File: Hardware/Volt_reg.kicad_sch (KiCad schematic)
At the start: 45 parts, among them Q2 BSZ025N04LS, Q3 BSZ025N04LS, Q4 BUK9M11-40EX, Q5 BUK9M11-40EX, U10 TPS55288QRPMRQ1, U8 INA219AxDCN, U9 LM74810

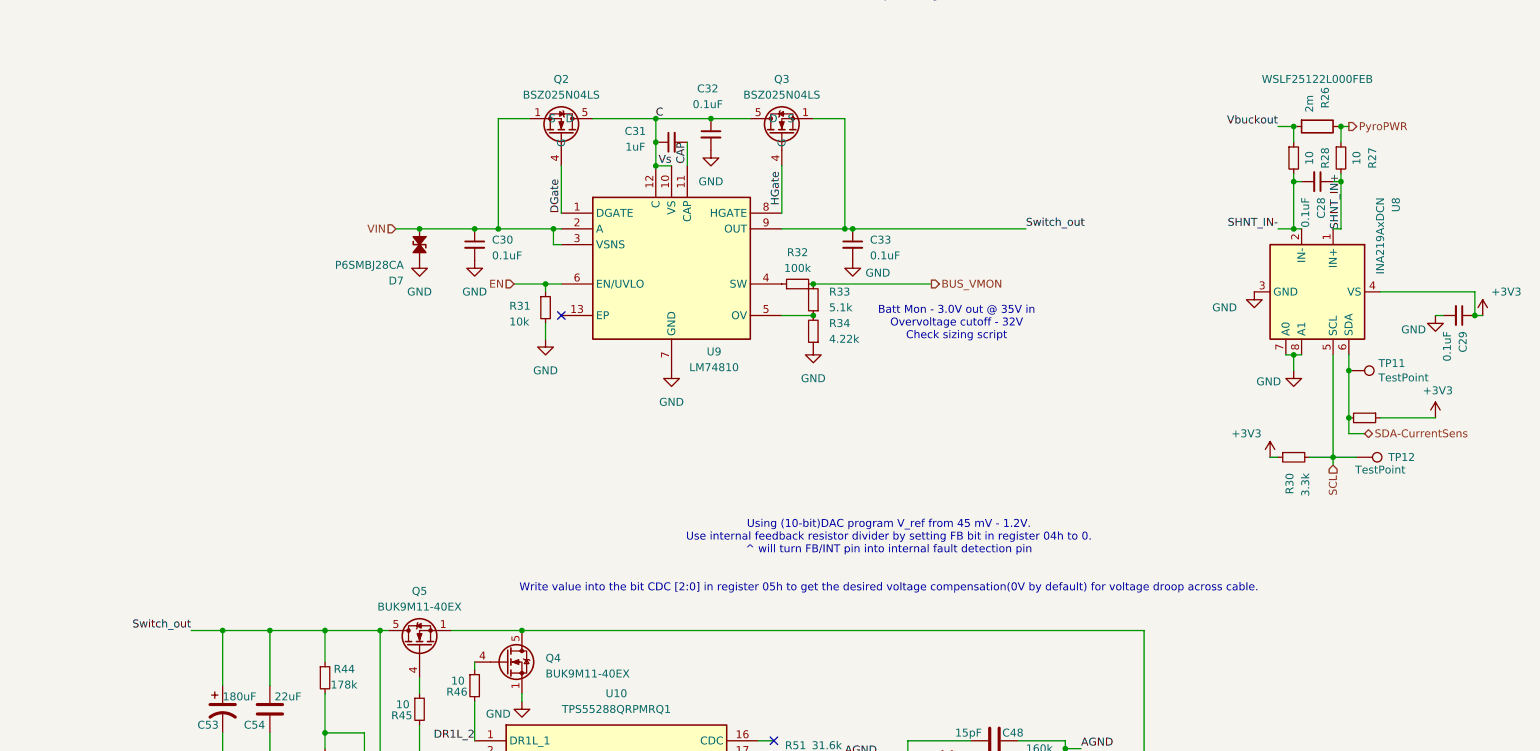
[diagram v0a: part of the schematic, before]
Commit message: Crosshair post review 2
Layout redesign + changes implemented. Traces not yet complete
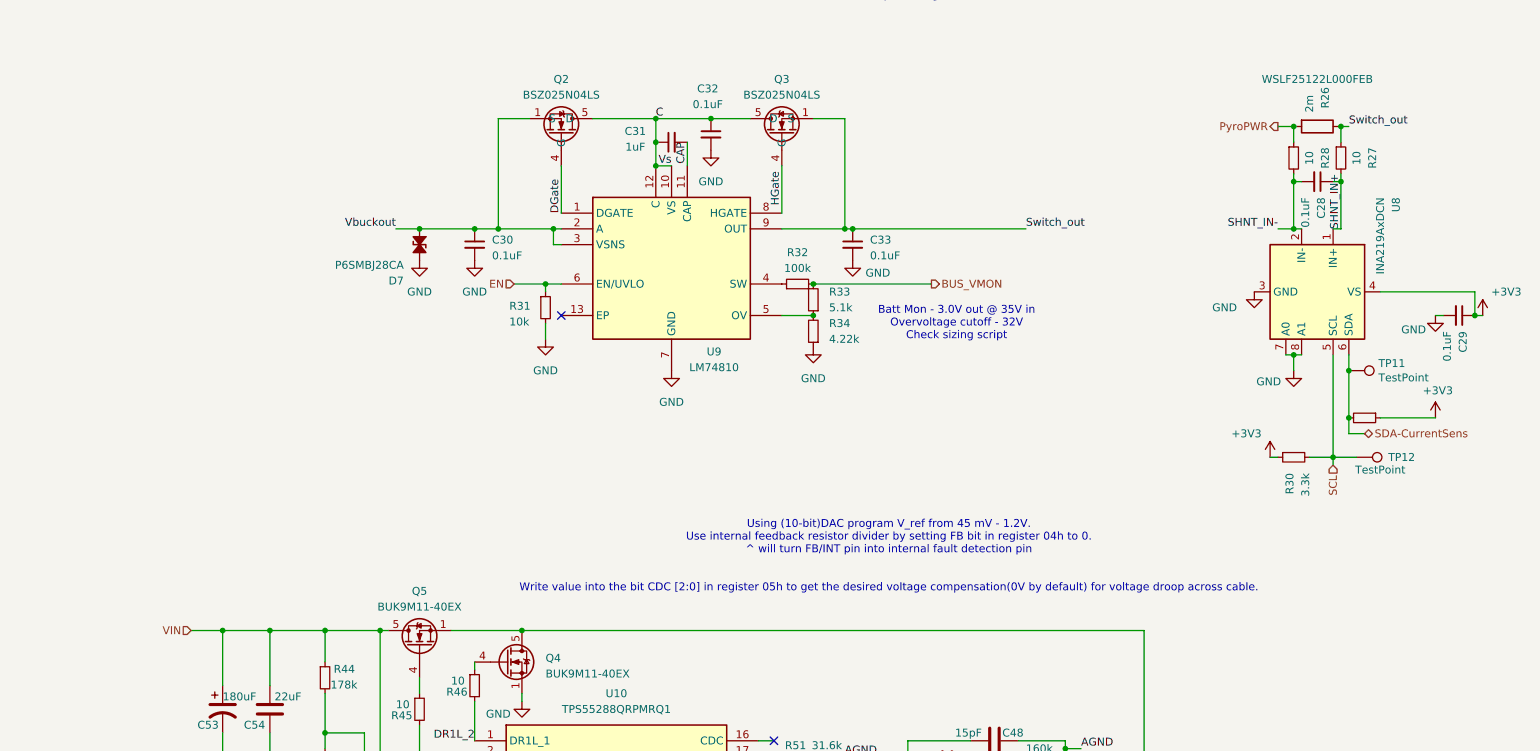
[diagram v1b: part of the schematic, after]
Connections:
- net ISN_2: now also C30.1, D7.1 (A1), Q2.1 (S), Q2.2 (S), Q2.3 (S), Q2.A1 (S), U9.2 (A), U9.3 (VSNS); no longer R26.2, R28.1
- net PyroPWR: now also R26.2, R28.1; no longer R26.1, R27.1
- net Switch_out: now also R26.1, R27.1; no longer C53.1, C54.2, Q5.5 (D), R44.1, U10.3 (VIN)
- net VIN: now also C53.1, C54.2, Q5.5 (D), R44.1, U10.3 (VIN); no longer C30.1, D7.1 (A1), Q2.1 (S), Q2.2 (S), Q2.3 (S), Q2.A1 (S), U9.2 (A), U9.3 (VSNS)
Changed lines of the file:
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@@
+		)
+	)
+	(label "Switch_out"
+		(at 213.36 55.88 0)
+		(effects
+			(font
+				(size 1.27 1.27)
+			)
+			(justify left bottom)
 		)
 	)
@@
 		)
 	)
-	(label "Vbuckout"
-		(at 201.93 55.88 180)
-		(effects
-			(font
-				(size 1.27 1.27)
-			)
-			(justify right bottom)
-		)
-	)
 	(label "DGate"
 		(at 86.36 69.85 90)
@@
 		)
 	)
-	(label "Switch_out"
-		(at 26.67 137.16 180)
-		(effects
-			(font
-				(size 1.27 1.27)
-			)
-			(justify right bottom)
-		)
-	)
 	(label "VCC_2"
 		(at 118.11 162.56 0)
@@
 			)
 			(justify left bottom)
+		)
+	)
+	(label "Vbuckout"
+		(at 59.69 72.39 180)
+		(effects
+			(font
+				(size 1.27 1.27)
+			)
+			(justify right bottom)
 		)
 	)
@@
 		)
 	)
-	(hierarchical_label "PyroPWR"
-		(shape output)
-		(at 213.36 55.88 0)
-		(effects
-			(font
-				(size 1.27 1.27)
-			)
-			(justify left)
-		)
-	)
 	(hierarchical_label "SDA-BuckBC"
 		(shape bidirectional)
@@
 	(hierarchical_label "VIN"
 		(shape input)
-		(at 59.69 72.39 180)
-		(effects
-			(font
+		(at 26.67 137.16 180)
+		(effects
+			(font
+				(size 1.27 1.27)
+			)
+			(justify right)
+		)
+	)
+	(hierarchical_label "PyroPWR"
+		(shape output)
+		(at 201.93 55.88 180)
+		(effects
+			(font

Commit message: Major changes made to layout
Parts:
- removed C30, C33: 0.1uF, Capacitor_SMD:C_0402_1005Metric, symbol Device:C_Small
- removed C31: 1uF, Capacitor_SMD:C_0402_1005Metric, symbol Device:C_Small
- removed C32: 0.1uF, Capacitor_SMD:C_0603_1608Metric, symbol Device:C_Small
- removed D7: P6SMBJ28CA, Diode_SMD:D_SMA, symbol Device:D_TVS_Small_Filled
- removed Q2, Q3: BSZ025N04LS, iclr:BSZ025N04LS, symbol iclr:BSZ025N04LS
- removed R31: 10k, Resistor_SMD:R_0402_1005Metric, symbol Device:R_Small
- removed R32: 100k, Resistor_SMD:R_0402_1005Metric, symbol Device:R_Small
- removed R33: 5.1k, Resistor_SMD:R_0402_1005Metric, symbol Device:R_Small
- removed R34: 4.22k, Resistor_SMD:R_0402_1005Metric, symbol Device:R_Small
- removed U9: LM74810, iclr:SON50P300X300X80-13N-D, symbol iclr:LM74810QDRRRQ1
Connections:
- net Switch_out is gone; now on net PyroPWR: R26.1, R27.1
- net ISN_2: now also R26.2, R28.1
- net PyroPWR: no longer R26.2, R28.1
- no-connect marks 2 -> 1
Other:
- note removed: "Batt Mon - 3.0V out @ 35V in Overvoltage cutoff - 32V Check sizing script"

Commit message: Saved changes
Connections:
- net ISN_2: now also R26.1, R27.1; no longer R26.2, R28.1
- net PyroPWR: now also R26.2, R28.1; no longer R26.1, R27.1
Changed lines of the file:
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@@
+		)
+	)
+	(label "Vbuckout"
+		(at 213.36 55.88 0)
+		(effects
+			(font
+				(size 1.27 1.27)
+			)
+			(justify left bottom)
 		)
 	)
@@
 	(label "ISN_2"
 		(at 72.39 185.42 180)
-		(effects
-			(font
-				(size 1.27 1.27)
-			)
-			(justify right bottom)
-		)
-	)
-	(label "Vbuckout"
-		(at 201.93 55.88 180)
 		(effects
 			(font
@@
 		)
 	)
+	(hierarchical_label "PyroPWR"
+		(shape output)
+		(at 201.93 55.88 180)
+		(effects
+			(font
+				(size 1.27 1.27)
+			)
+			(justify right)
+		)
+	)
 	(hierarchical_label "SCL"
 		(shape input)
@@
 		)
 	)
-	(hierarchical_label "PyroPWR"
-		(shape output)
-		(at 213.36 55.88 0)
-		(effects
-			(font
-				(size 1.27 1.27)
-			)
-			(justify left)
-		)
-	)

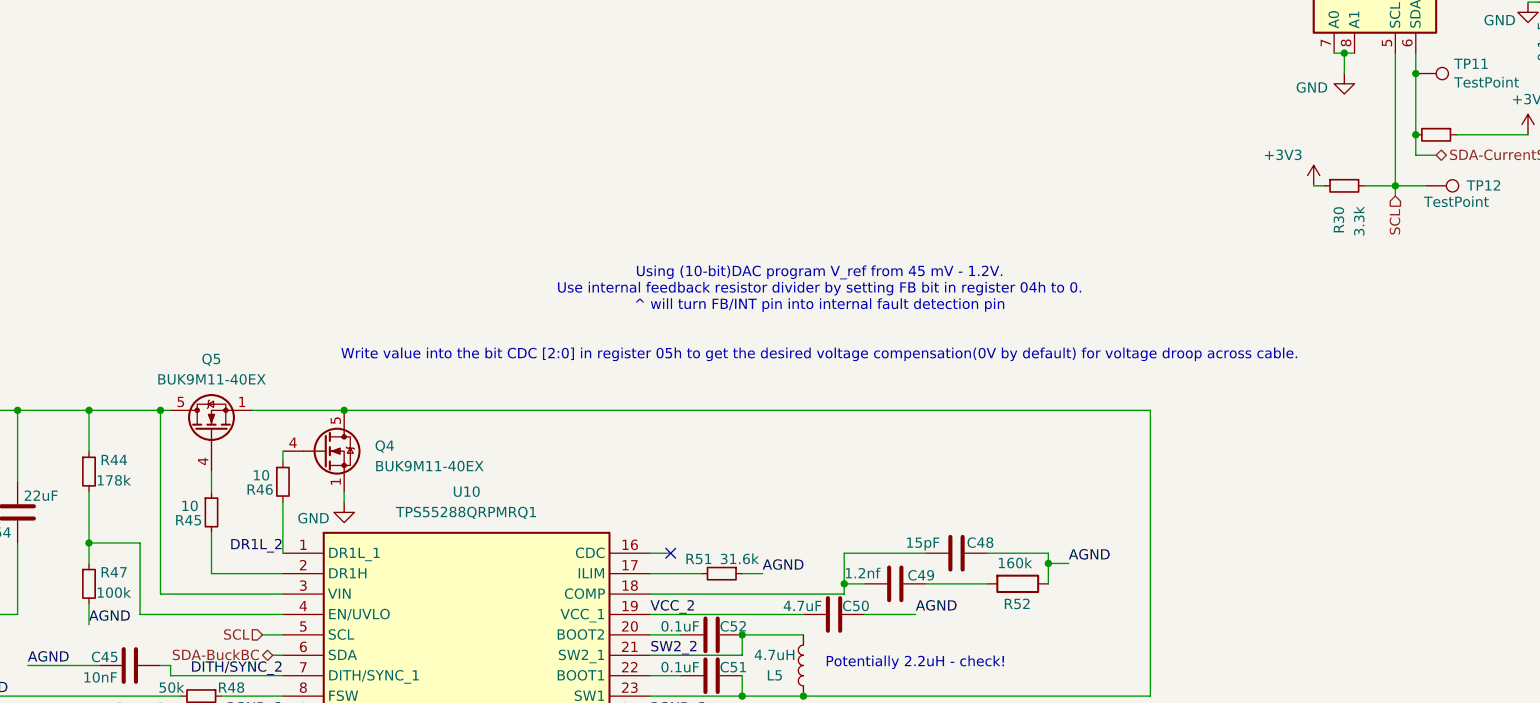
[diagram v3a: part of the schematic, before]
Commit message: GPIO broken out + post review 4
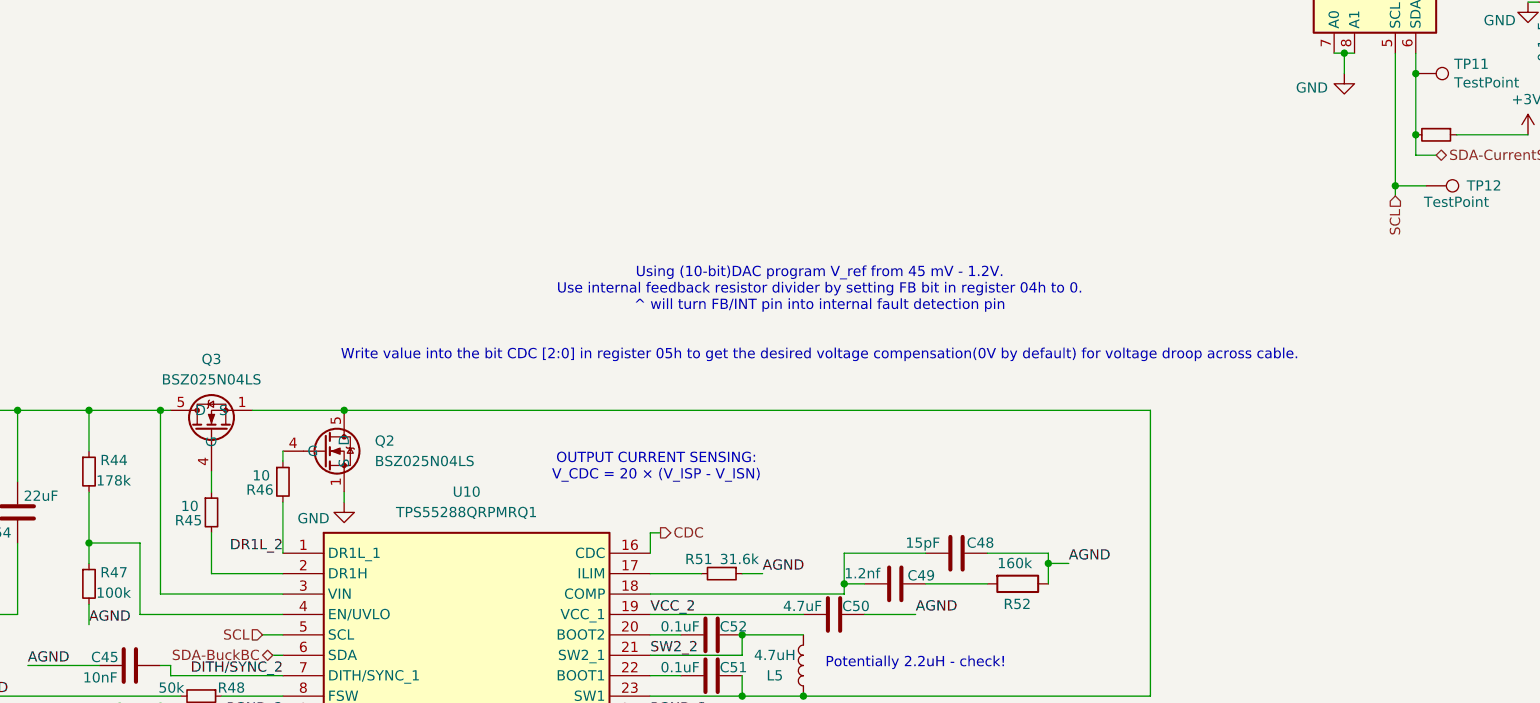
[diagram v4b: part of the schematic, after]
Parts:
- removed Q4, Q5: BUK9M11-40EX, Package_TO_SOT_SMD:LFPAK33, symbol Transistor_FET:BUK9M11-40EX
- removed R30: 3.3k, Resistor_SMD:R_0402_1005Metric, symbol Device:R_Small
- added Q2, Q3: BSZ025N04LS, iclr:BSZ025N04LS, symbol iclr:BSZ025N04LS
- R49: footprint Resistor_SMD:R_0402_1005Metric -> Resistor_SMD:R_1206_3216Metric
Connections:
- net GND: now also Q2.1 (S), Q2.2 (S), Q2.3 (S), Q2.A1 (S)
- net VIN: now also Q3.5 (D), Q3.6 (D), Q3.7 (D), Q3.8 (D), Q3.A5 (D)
- net at C51.1, L5.1, U10.23 (SW1): now also Q2.5 (D), Q2.6 (D), Q2.7 (D), Q2.8 (D), Q2.A5 (D), Q3.1 (S), Q3.2 (S), Q3.3 (S), Q3.A1 (S)
- net at R46.1: now also Q2.4 (G)
- net at R45.1: now also Q3.4 (G)
- net CDC: now reaches U10.16 (CDC)
- no-connect marks 1 -> 0
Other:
- note added: "OUTPUT CURRENT SENSING: V_CDC = 20 × (V_ISP - V_ISN)"

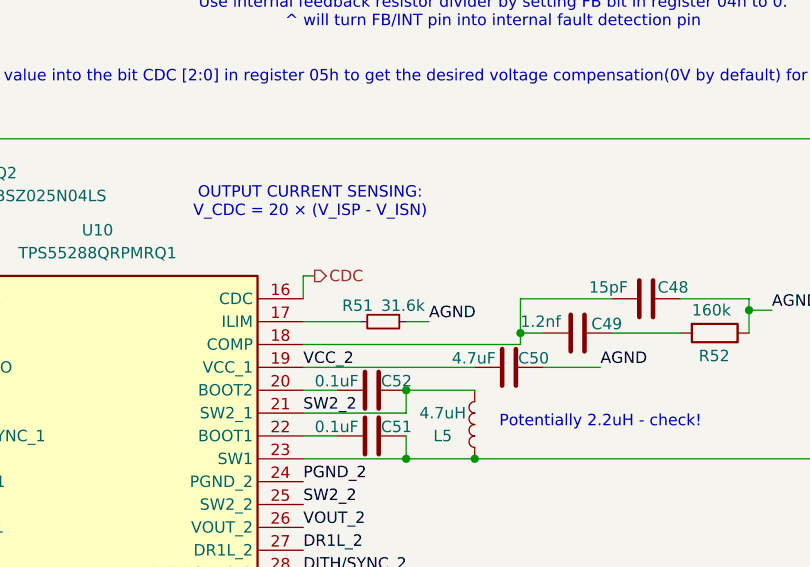
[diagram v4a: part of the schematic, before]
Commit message: Changed mosfet + added top plane for Cell_+ and fixed silkscreen
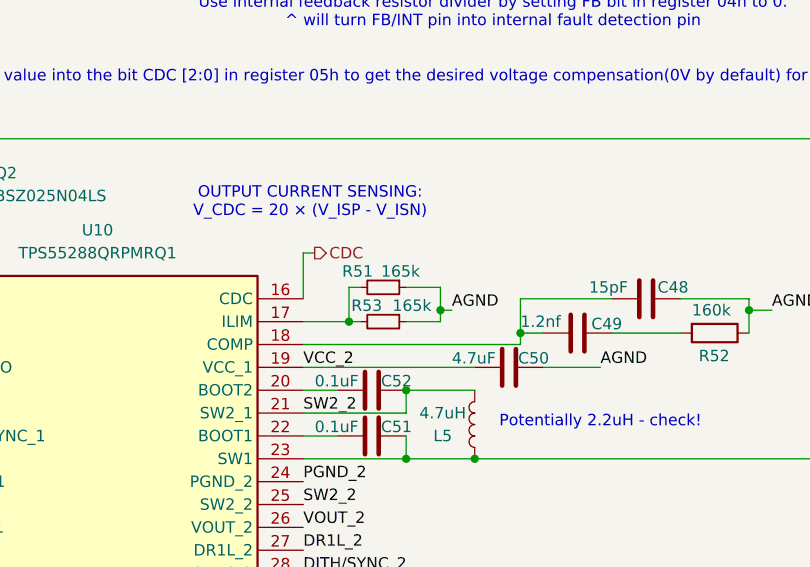
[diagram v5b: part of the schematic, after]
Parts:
- added R53: 165k, Resistor_SMD:R_0402_1005Metric, symbol Device:R_Small
- R51: value 31.6k -> 165k
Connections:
- net GND: now also R53.1
- net at R51.2, U10.17 (ILIM): now also R53.2
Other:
- moved on the sheet: R51
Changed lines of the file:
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@@
 	)
 	(junction
+		(at 123.19 157.48)
+		(diameter 0)
+		(color 0 0 0 0)
+	)
+	(junction
 		(at 57.15 181.61)
 		(diameter 0)
@@
 	)
 	(junction
+		(at 133.35 156.21)
+		(diameter 0)
+		(color 0 0 0 0)
+	)
+	(junction
 		(at 204.47 92.71)
 		(diameter 0)
@@
 	(wire
 		(pts
-			(xy 129.54 157.48) (xy 132.08 157.48)
+			(xy 129.54 153.67) (xy 133.35 153.67)
 		)
 		(stroke
@@
 	(wire
 		(pts
+			(xy 133.35 153.67) (xy 133.35 156.21)
+		)
+		(stroke
+			(width 0)
+			(type default)
+		)
+	)
+	(wire
+		(pts
 			(xy 46.99 190.5) (xy 53.34 190.5)
 		)
@@
 	(wire
 		(pts
-			(xy 118.11 152.4) (xy 119.38 152.4)
+			(xy 118.11 149.86) (xy 119.38 149.86)
 		)
 		(stroke
@@
 	(wire
 		(pts
+			(xy 134.62 156.21) (xy 133.35 156.21)
+		)
+		(stroke
+			(width 0)
+			(type default)
+		)
+	)
+	(wire
+		(pts
+			(xy 123.19 157.48) (xy 118.11 157.48)
+		)
+		(stroke
+			(width 0)
+			(type default)
+		)
+	)
+	(wire
+		(pts
 			(xy 57.15 181.61) (xy 52.07 181.61)
 		)
@@
 	(wire
 		(pts
+			(xy 133.35 156.21) (xy 133.35 157.48)
+		)
+		(stroke
+			(width 0)
+			(type default)
+		)
+	)
+	(wire
+		(pts
 			(xy 201.93 72.39) (xy 204.47 72.39)
 		)
@@
 	(wire
 		(pts
+			(xy 123.19 153.67) (xy 123.19 157.48)
+		)
+		(stroke
+			(width 0)
+			(type default)
+		)
+	)
+	(wire
+		(pts
+			(xy 124.46 157.48) (xy 123.19 157.48)
+		)
+		(stroke
+			(width 0)
+			(type default)
+		)
+	)
+	(wire
+		(pts
+			(xy 129.54 157.48) (xy 133.35 157.48)
+		)
+		(stroke
+			(width 0)
+			(type default)
+		)
+	)
+	(wire
+		(pts
 			(xy 212.09 55.88) (xy 212.09 58.42)
 		)
@@
 	(wire
 		(pts
-			(xy 118.11 152.4) (xy 118.11 154.94)
+			(xy 118.11 149.86) (xy 118.11 154.94)
 		)
 		(stroke
@@
 	(wire
 		(pts
-			(xy 118.11 157.48) (xy 124.46 157.48)
+			(xy 123.19 153.67) (xy 124.46 153.67)
 		)
 		(stroke
@@
 	)
 	(label "AGND"
-		(at 132.08 157.48 0)
+		(at 134.62 156.21 0)
 		(effects
 			(font
@@
 	(hierarchical_label "CDC"
 		(shape output)
-		(at 119.38 152.4 0)
+		(at 119.38 149.86 0)
 		(effects
 			(font
@@
 	)
 	(symbol
+		(lib_id "Device:R_Small")
+		(at 127 157.48 270)
+		(unit 1)
+		(exclude_from_sim no)
+		(in_bom yes)
+		(on_board yes)
+		(dnp no)
+		(property "Reference" "R53"
+			(at 123.444 155.702 90)
+			(effects
+				(font
+					(size 1.27 1.27)
+				)
+				(justify left)
+			)
+		)
+		(property "Value" "165k"
+			(at 128.016 155.702 90)
+			(effects
+				(font
+					(size 1.27 1.27)
+				)
+				(justify left)
+			)
+		)
+		(property "Footprint" "Resistor_SMD:R_0402_1005Metric"
+			(at 127 157.48 0)
+			(effects
+				(font
+					(size 1.27 1.27)
+				)
+				(hide yes)
+			)
+		)
+		(property "Datasheet" "~"
+			(at 127 157.48 0)
+			(effects
+				(font
+					(size 1.27 1.27)
+				)
+				(hide yes)
+			)
+		)
+		(property "Description" "Resistor, small symbol"
+			(at 127 157.48 0)
+			(effects
+				(font
+					(size 1.27 1.27)
+				)
+				(hide yes)
+			)
+		)
+		(pin "1"
+		)
+		(pin "2"
+		)
+		(instances
+			(project "Main board"
+				(path "/7db990e4-92e1-4f99-b4d2-435bbec1ba83/ab7b921d-66d3-49d7-abff-63184671bf46"
+					(reference "R53")
+					(unit 1)
+				)
+			)
+		)
+	)
+	(symbol
 		(lib_id "Device:R")
 		(at 163.83 158.75 270)
@@
 	(symbol
 		(lib_id "Device:R_Small")
-		(at 127 157.48 270)
+		(at 127 153.67 270)
 		(unit 1)
 		(exclude_from_sim no)
@@
 		(dnp no)
 		(property "Reference" "R51"
-			(at 122.428 155.702 90)
+			(at 122.428 151.892 90)
 			(effects
 				(font
@@
 			)
 		)
-		(property "Value" "31.6k"
-			(at 126.746 155.702 90)
+		(property "Value" "165k"
+			(at 126.746 151.892 90)
 			(effects
 				(font
@@
 		)
 		(property "Footprint" "Resistor_SMD:R_0402_1005Metric"
-			(at 127 157.48 0)
+			(at 127 153.67 0)
 			(effects
 				(font
@@
 		)
 		(property "Datasheet" "~"
-			(at 127 157.48 0)
+			(at 127 153.67 0)
 			(effects
 				(font
@@
 		)
 		(property "Description" "Resistor, small symbol"
-			(at 127 157.48 0)
+			(at 127 153.67 0)
 			(effects
 				(font

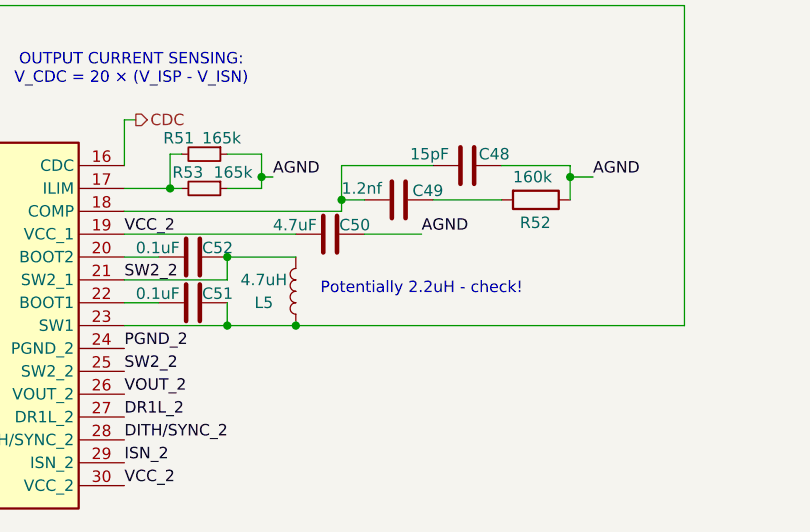
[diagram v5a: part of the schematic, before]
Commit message: Changed buck boost inductor + changed planes and vias
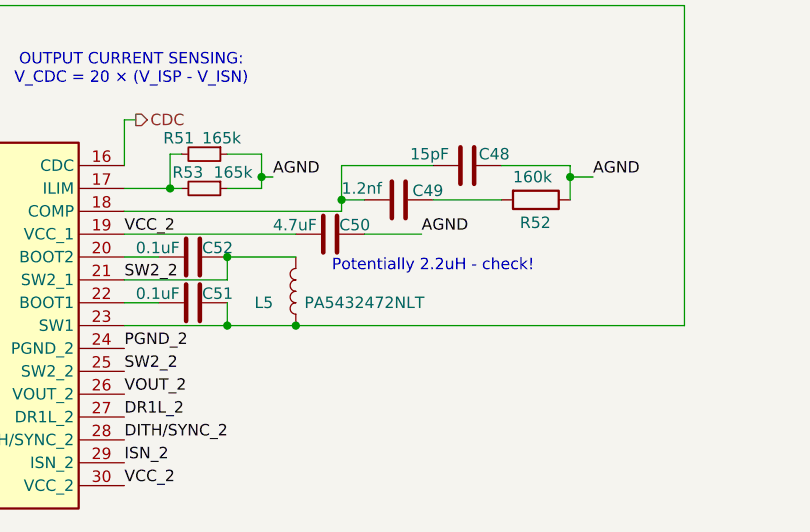
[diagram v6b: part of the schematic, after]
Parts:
- L5: value 4.7uH -> PA5432472NLT; footprint Inductor_SMD:L_10.4x10.4_H4.8 -> iclr:PA5432472NLT; Inductance (none) -> 4.7uH
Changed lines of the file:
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@@
 	(text "Potentially 2.2uH - check!"
 		(exclude_from_sim no)
-		(at 151.13 168.656 0)
+		(at 152.4 166.116 0)
 		(effects
 			(font
@@
 			)
 		)
-		(property "Value" "4.7uH"
-			(at 133.604 167.64 0)
+		(property "Value" "PA5432472NLT"
+			(at 144.78 170.18 0)
 			(effects
 				(font
@@
 			)
 		)
-		(property "Footprint" "Inductor_SMD:L_10.4x10.4_H4.8"
+		(property "Footprint" "iclr:PA5432472NLT"
 			(at 137.16 168.91 0)
 			(effects
@@
 			(at 137.16 168.91 0)
 			(effects
+				(font
+					(size 1.27 1.27)
+				)
+				(hide yes)
+			)
+		)
+		(property "Inductance" "4.7uH"
+			(at 137.16 168.91 0)
+			(effects
